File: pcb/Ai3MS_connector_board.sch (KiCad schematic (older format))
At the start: 9 parts, among them J1 2x7, J2 1x4_rev, J3 1x3_rev, T0 1x2

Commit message: Export symbols and footprints to libraries
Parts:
- BLTOUCH1: symbol mogira:1x5 -> Ai3MS_connector_board:1x5
- EXTRUDER1: symbol mogira:1x4 -> Ai3MS_connector_board:1x4
- FAN0, FAN2, HOTEND1, T0: symbol mogira:1x2 -> Ai3MS_connector_board:1x2
- J1: footprint mogira:PHLike_Green_Connector -> Ai3MS_connector_board:PHLike_Green_Connector; symbol mogira:2x7 -> Ai3MS_connector_board:2x7
- J2: symbol mogira:1x4_rev -> Ai3MS_connector_board:1x4_rev
- J3: symbol mogira:1x3_rev -> Ai3MS_connector_board:1x3_rev
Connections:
- net BLTOUCH1_BLUE: now also J1.11 (Pin_11), J1.12 (Pin_12); no longer J1.6 (Pin_6), J1.9 (Pin_9)
- net BLTOUCH1_WHITE: now also J1.9 (Pin_9); no longer J1.5 (Pin_5)
- net FAN0_P1: now also J1.3 (Pin_3); no longer J1.14 (Pin_14)
- net FAN0_P2: now also J1.8 (Pin_8); no longer J1.11 (Pin_11)
- net FAN2_P2: now also J1.6 (Pin_6); no longer J1.12 (Pin_12)
- net HOTEND1_P1: now also J1.5 (Pin_5), J1.7 (Pin_7); no longer J1.13 (Pin_13), J1.3 (Pin_3)
- net T0_P1: now also J1.13 (Pin_13), J1.14 (Pin_14); no longer J1.7 (Pin_7), J1.8 (Pin_8)
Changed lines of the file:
@@
 	2750 4850 3350 4850
 $Comp
-L mogira:1x2 FAN2
+L Ai3MS_connector_board:1x2 FAN2
 U 1 1 5F10A633
 P 2600 2850
@@
 $EndComp
 $Comp
-L mogira:1x2 FAN0
+L Ai3MS_connector_board:1x2 FAN0
 U 1 1 5F10AA55
 P 2600 2300
@@
 T0_P1
 $Comp
-L mogira:1x2 T0
+L Ai3MS_connector_board:1x2 T0
 U 1 1 5F10AE6F
 P 3800 2300
@@
 Connection ~ 2650 4200
 $Comp
-L mogira:2x7 J1
+L Ai3MS_connector_board:2x7 J1
 U 1 1 5F1093E7
 P 3050 4300
 F 0 "J1" H 3050 4400 50  0000 C CNN
 F 1 "2x7" H 3050 4250 25  0000 C CNN
-F 2 "mogira:PHLike_Green_Connector" H 3050 4250 50  0001 C CNN
+F 2 "Ai3MS_connector_board:PHLike_Green_Connector" H 3050 4250 50  0001 C CNN
 F 3 "" H 3050 4250 50  0001 C CNN
 	1    3050 4300
@@
 T0_P2
 $Comp
-L mogira:1x2 HOTEND1
+L Ai3MS_connector_board:1x2 HOTEND1
 U 1 1 5F109B81
 P 3800 2850
@@
 $EndComp
 $Comp
-L mogira:1x4_rev J2
+L Ai3MS_connector_board:1x4_rev J2
 U 1 1 5F1321D5
 P 4400 2450
@@
 BLTOUCH1_BROWN
 $Comp
-L mogira:1x5 BLTOUCH1
+L Ai3MS_connector_board:1x5 BLTOUCH1
 U 1 1 5F179B7D
 P 7050 2650
@@
 $EndComp
 $Comp
-L mogira:1x3_rev J3
+L Ai3MS_connector_board:1x3_rev J3
 U 1 1 5F1884C2
 P 5850 2750
@@
 	4500 2300 4750 2300
 $Comp
-L mogira:1x4 EXTRUDER1
+L Ai3MS_connector_board:1x4 EXTRUDER1
 U 1 1 5F12BC10
 P 4850 2450

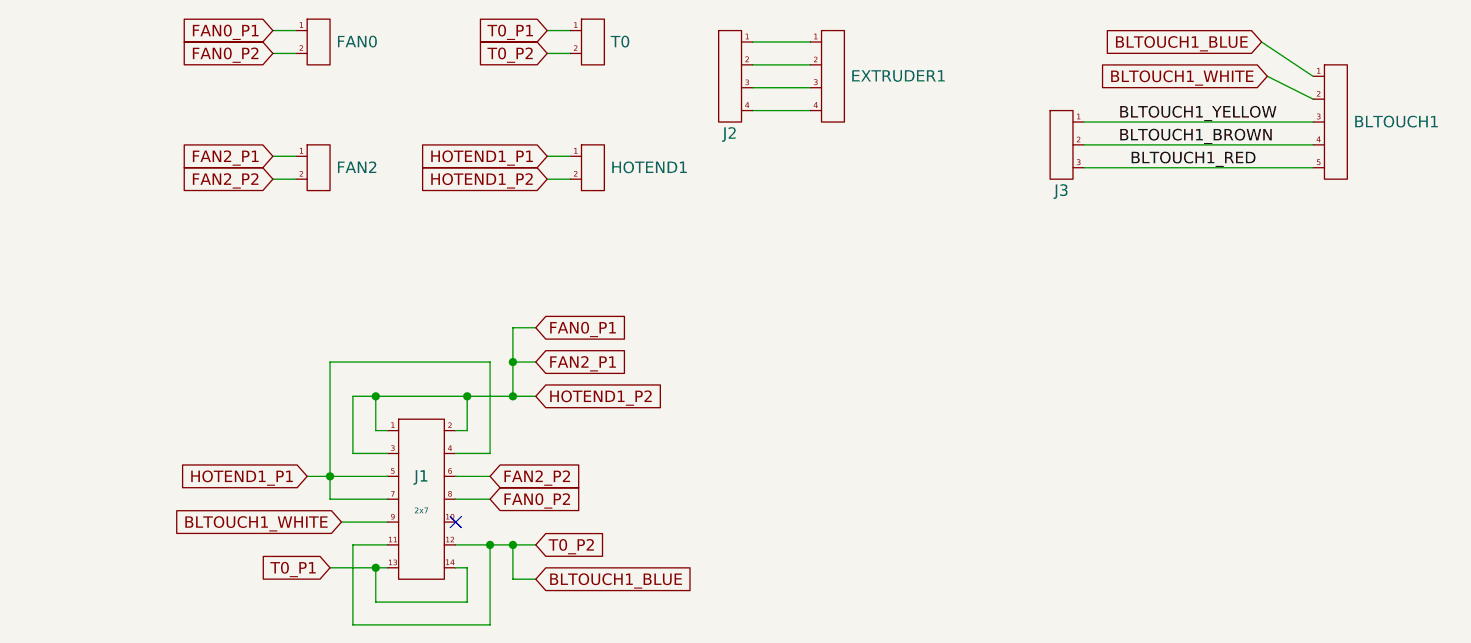
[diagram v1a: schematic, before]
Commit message: Improve links
* Change link names
* Change connection paths
* Retouch PCB due to loading new net file

* Note: HEATER's 12V/GND is inversed of others. Pin#1 is GND, Pin#2 is 12V.
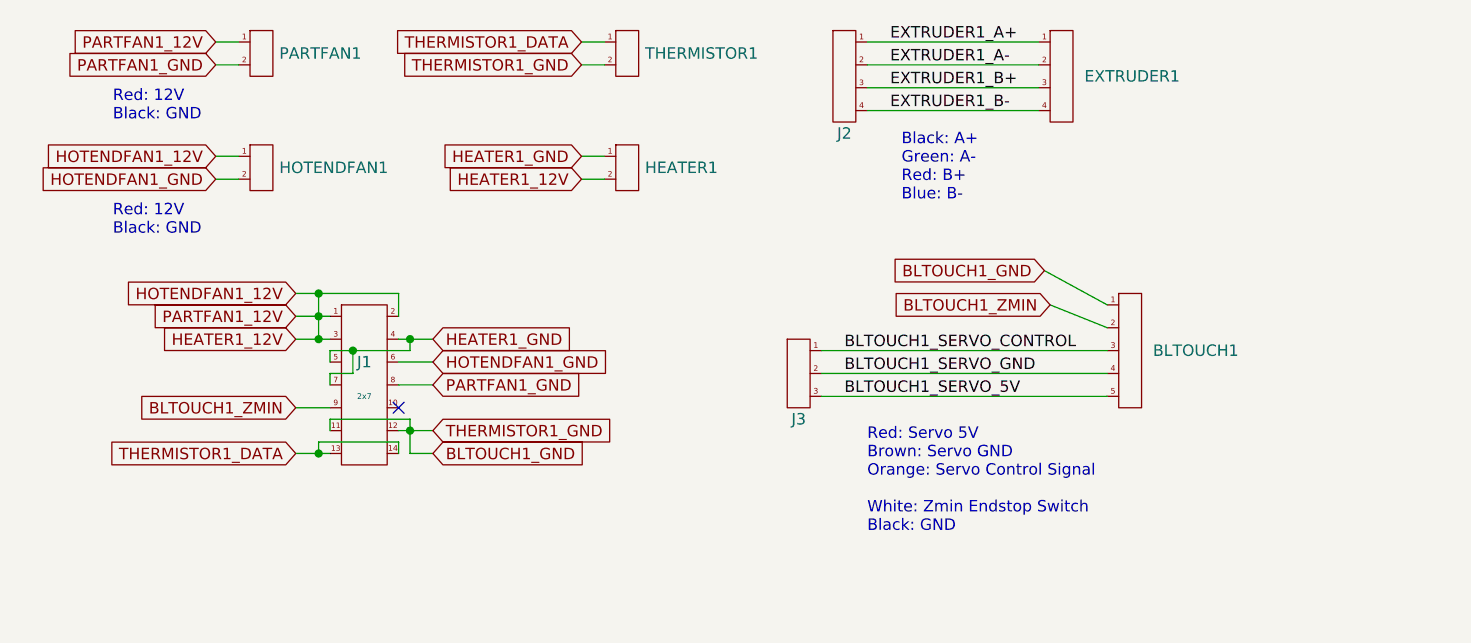
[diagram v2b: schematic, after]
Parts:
- renumbered HOTEND1 to HEATER1, FAN2 to HOTENDFAN1, FAN0 to PARTFAN1, T0 to THERMISTOR1
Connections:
- net EXTRUDER1_A+: now reaches EXTRUDER1.1 (Pin_1), J2.1 (Pin_1)
- net EXTRUDER1_A-: now reaches EXTRUDER1.2 (Pin_2), J2.2 (Pin_2)
- net EXTRUDER1_B+: now reaches EXTRUDER1.3 (Pin_3), J2.3 (Pin_3)
- net EXTRUDER1_B-: now reaches EXTRUDER1.4 (Pin_4), J2.4 (Pin_4)
- net BLTOUCH1_BLUE renamed BLTOUCH1_GND
- net BLTOUCH1_BROWN renamed BLTOUCH1_SERVO_GND
- net BLTOUCH1_RED renamed BLTOUCH1_SERVO_5V
- net BLTOUCH1_WHITE renamed BLTOUCH1_ZMIN
- net BLTOUCH1_YELLOW renamed BLTOUCH1_SERVO_CONTROL
- net FAN0_P1 renamed HEATER1_12V
- net FAN0_P2 renamed PARTFAN1_GND
- net FAN2_P2 renamed HOTENDFAN1_GND
- net HOTEND1_P1 renamed HEATER1_GND
- net T0_P1 renamed THERMISTOR1_DATA
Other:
- note added: "Black: A+\nGreen: A-\nRed: B+\nBlue: B-"
- note added: "Red: 12V\nBlack: GND"
- note added: "Red: Servo 5V\nBrown: Servo GND\nOrange: Servo Control Signal\n\nWhite: Zmin Endstop Switch\nBlack: GND"
- moved on the sheet: BLTOUCH1, EXTRUDER1, HEATER1, HOTENDFAN1, J1, J2, J3, PARTFAN1, THERMISTOR1

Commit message: Improve 2x7_2mm-pitch_Lock_GreenConnector
* Renamed from "PHLike_Green_Connector"
* Fix pin assign of symbol "2x7"
* Fix pin assign of footprint "2x7_2mm-pitch_Lock_GreenConnector"
* Update silk
* Add 3d model
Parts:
- J1: footprint Ai3MS_connector_board:PHLike_Green_Connector -> Ai3MS_connector_board:2x7_2mm-pitch_Lock_GreenConnector
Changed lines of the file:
@@
 F 0 "J1" H 2800 3900 50  0000 C CNN
 F 1 "2x7" H 2800 3750 25  0000 C CNN
-F 2 "Ai3MS_connector_board:PHLike_Green_Connector" H 2800 3750 50  0001 C CNN
+F 2 "Ai3MS_connector_board:2x7_2mm-pitch_Lock_GreenConnector" H 2800 3750 50  0001 C CNN
 F 3 "" H 2800 3750 50  0001 C CNN
 	1    2800 3800
